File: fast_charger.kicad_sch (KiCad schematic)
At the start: 36 parts, among them J1 Screw_Terminal_01x02, J2 USB_A, J3 AVR-ISP-6, J4 Conn_02x08_Counter_Clockwise, Q1 PJD25N03, U1 CHY100, U2 IRS10752LVBF, U3 ATtiny404-SS, U4 AP7375, U5 AP7375, U6 INA180A4

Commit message: Completed BOM
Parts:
- removed C1, C2: C, symbol Device:C
- removed D1: D, symbol Device:D
- added C1: 10n, Capacitor_SMD:C_0603_1608Metric, symbol Device:C_Small
- added C10, C11, C9: 100u, Capacitor_SMD:CP_Elec_10x10.5, symbol Device:C_Polarized_US
- added D1: SBM54, Diode_SMD:D_SMA, symbol Device:D_Schottky
- added D3: RED, Diode_SMD:D_0603_1608Metric, symbol Device:LED
- added D4: YEL, Diode_SMD:D_0603_1608Metric, symbol Device:LED
- added D5: GRN, Diode_SMD:D_0603_1608Metric, symbol Device:LED
- added R13, R14, R15: 1k, Resistor_SMD:R_0603_1608Metric, symbol Device:R_US
- C3, C4, C5, C6, C7, C8: footprint (none) -> Capacitor_SMD:C_0603_1608Metric
- D2: value D_Schottky -> SBM54; footprint (none) -> Diode_SMD:D_SMA
- J1: footprint (none) -> TerminalBlock_Phoenix:TerminalBlock_Phoenix_MKDS-3-2-5.08_1x02_P5.08mm_Horizontal
- J2: footprint (none) -> fast_charger:usb_CU01
- J3: footprint (none) -> Connector_IDC:IDC-Header_2x03_P2.54mm_Vertical
- J4: footprint (none) -> Connector_PinHeader_1.27mm:PinHeader_1x16_P1.27mm_Vertical
- L1: value L -> 47u; footprint (none) -> fast_charger:L_murata_6000B
- R1, R10, R11, R2, R3, R5, R6, R7, R8, R9: footprint (none) -> Resistor_SMD:R_0603_1608Metric
- R12: value 25m -> 20m; footprint (none) -> Resistor_SMD:R_1206_3216Metric
- R4: value R_US -> 100k; footprint (none) -> Resistor_SMD:R_0603_1608Metric
- TP1, TP2: footprint (none) -> TestPoint:TestPoint_THTPad_D1.5mm_Drill0.7mm
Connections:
- net GND: now also C1.2, C10.2, C11.2, C9.2, D3.1 (K), D4.1 (K), D5.1 (K)
- net VDD: now also C9.1
- net at C4.1, C5.1, R6.1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: now also D1.2 (A)
- net VSW: now reaches C3.2, D2.1 (K), L1.1, Q1.2 (D), U2.4 (VS)
- net at L1.2, R12.1, U6.3 (+): now also C1.1, C10.1, C11.1
- net at C3.1, TP2.1, U2.6 (VB): now also D1.1 (K)
- net AUX_ANALOG: now reaches J4.16 (Pin_16)
- net ~{RST}: now reaches J3.5 (~{RST}), U3.10 (~{RESET}/PA0)
- net MOSI: now reaches J3.4 (MOSI), U3.11 (PA1)
- net MOSI: now also R14.1
- net MISO: now reaches J3.1 (MISO), U3.12 (PA2)
- net MISO: now also R13.1
- net SCK: now reaches J3.3 (SCK), U3.13 (PA3)
- net SCK: now also R15.1
- net SW renamed PWM
- new net: D4.2 (A), R14.2
- new net: D3.2 (A), R13.2
- new net: D5.2 (A), R15.2
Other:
- note added: "LEDs for diagnostics and communication"
- moved on the sheet: J1, J2, J3, R1, R12, R2, R3, R4, TP2, U1, U6

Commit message: Completed placement
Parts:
- added D6: SBM54, Diode_SMD:D_SMA, symbol Device:D_Schottky
- added J5: Conn_02x03_Odd_Even, Connector_PinHeader_1.27mm:PinHeader_2x03_P1.27mm_Vertical, symbol Connector_Generic:Conn_02x03_Odd_Even
- added Q2: PJD25N03, Package_TO_SOT_SMD:TO-252-2, symbol Device:Q_NMOS_GDS
- J4: value Conn_02x08_Counter_Clockwise -> Conn_02x08_Odd_Even; footprint Connector_PinHeader_1.27mm:PinHeader_1x16_P1.27mm_Vertical -> Connector_PinHeader_1.27mm:PinHeader_2x08_P1.27mm_Vertical; symbol Connector_Generic:Conn_02x08_Counter_Clockwise -> Connector_Generic:Conn_02x08_Odd_Even
- R1: value 100k -> 400k
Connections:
- net +5V: now also J5.1 (Pin_1), J5.3 (Pin_3), J5.5 (Pin_5); no longer R2.2, R3.2
- net AUX_ANALOG: now also J4.2 (Pin_2); no longer J4.16 (Pin_16)
- net GND: now also J5.2 (Pin_2), J5.4 (Pin_4), J5.6 (Pin_6), Q2.3 (S)
- net PWM: now also J4.16 (Pin_16); no longer J4.9 (Pin_9)
- net at C7.1, R8.2, R9.1: now also J4.8 (Pin_8); no longer J4.13 (Pin_13)
- net at C1.1, C10.1, C11.1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: now also D6.1 (K); no longer L1.2
- net at C8.1, R10.2, R11.1: now also J4.6 (Pin_6); no longer J4.14 (Pin_14)
- net at U3.3 (PA5): now also J4.3 (Pin_3); no longer J4.2 (Pin_2)
- net at U3.4 (PA6): now also J4.5 (Pin_5); no longer J4.3 (Pin_3)
- net at U3.5 (PA7): now also J4.7 (Pin_7); no longer J4.4 (Pin_4)
- net at U3.6 (PB3): now also J4.9 (Pin_9); no longer J4.5 (Pin_5)
- net at U3.7 (PB2): now also J4.11 (Pin_11); no longer J4.6 (Pin_6)
- net at U3.8 (PB1): now also J4.13 (Pin_13); no longer J4.7 (Pin_7)
- net at U3.9 (PB0): now also J4.15 (Pin_15); no longer J4.8 (Pin_8)
- net IL renamed ILOAD
- net ILOAD: now also J4.4 (Pin_4); no longer J4.15 (Pin_15)
- net ~{N1} renamed REQ_V
- net REQ_V: now also R3.2, U1.4 (V3); no longer U1.2 (V1)
- removed net ~{N2}: J4.11 (Pin_11), R2.1, U1.3 (V2)
- removed net ~{N3}: J4.12 (Pin_12), R3.1, U1.4 (V3)
- new net: D6.2 (A), L1.2, Q2.2 (D)
- new net: R2.1, U1.2 (V1)
- new net: R2.2, R3.1, U1.3 (V2)
- new net PWM2: J4.14 (Pin_14), Q2.1 (G)
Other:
- note added: "REQ_V | Requested Charge Voltage 5V | 5V 1.6V | 9V 1.0V | 12V 0V | 20V"
- moved on the sheet: C1, C10, C11, C3, C4, C5, C6, C7, C8, C9, D1, D2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

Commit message: V1 complete. PCB and parts ordered
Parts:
- D1: value SBM54 -> 1N4148W; footprint Diode_SMD:D_SMA -> Diode_SMD:D_SOD-123
- R6: value 100k -> 4.7k
- R7: value 200k -> 10k
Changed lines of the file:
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@@
       (effects (font (size 1.27 1.27)) (justify right))
     )
-    (property "Value" "SBM54" (at 152.4 86.6775 90)
-      (effects (font (size 1.27 1.27)) (justify right))
-    )
-    (property "Footprint" "Diode_SMD:D_SMA" (at 154.94 85.09 0)
+    (property "Value" "1N4148W" (at 152.4 86.6775 90)
+      (effects (font (size 1.27 1.27)) (justify right))
+    )
+    (property "Footprint" "Diode_SMD:D_SOD-123" (at 154.94 85.09 0)
       (effects (font (size 1.27 1.27)) hide)
     )
@@
       (effects (font (size 1.27 1.27)) (justify left))
     )
-    (property "Value" "200k" (at 125.73 96.52 0)
+    (property "Value" "10k" (at 125.73 96.52 0)
       (effects (font (size 1.27 1.27)) (justify left))
     )
@@
       (effects (font (size 1.27 1.27)) (justify left))
     )
-    (property "Value" "100k" (at 120.65 87.63 0)
-      (effects (font (size 1.27 1.27)) (justify left))
-    )
+    (property "Value" "4.7k" (at 120.65 87.63 0)
+      (effects (font (size 1.27 1.27)) (justify left))
+    )

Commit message: Too many issues. Moving to a simpler design
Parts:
- removed C5: 10n, Capacitor_SMD:C_0603_1608Metric, symbol Device:C_Small
- removed R6: 4.7k, Resistor_SMD:R_0603_1608Metric, symbol Device:R_US
- removed R7: 10k, Resistor_SMD:R_0603_1608Metric, symbol Device:R_US
- removed U4: AP7375, Package_TO_SOT_SMD:SOT-23, symbol Regulator_Linear:AP7384-28SA
- added D7, D8: 1N4148W, Diode_SMD:D_SOD-123, symbol Device:D_Schottky
- R10, R8: value 400k -> 100k
- R11, R9: value 100k -> 10k
- R12: value 20m -> 5m
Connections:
- net VBUS: now also D8.2 (A)
- net VDD: now also C4.1, D1.2 (A), TP1.1, U2.1 (VCC), D7.1 (K), D8.1 (K); no longer C9.1, J1.1 (Pin_1), Q1.3 (S)
- net VSW: now also Q1.3 (S); no longer Q1.2 (D)
- new net: C9.1, D7.2 (A), J1.1 (Pin_1), Q1.2 (D)
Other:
- note added: "Order of testing * Voltage regulators * High-side switch * Low-side switch * Voltage dividers * Current measurement * USB charge negotiation --- Firmware --- * High-side switch * Low-side switch * Analog inputs * Buck regulation * Boost regulation * Maximum power delivery"
- moved on the sheet: Q1

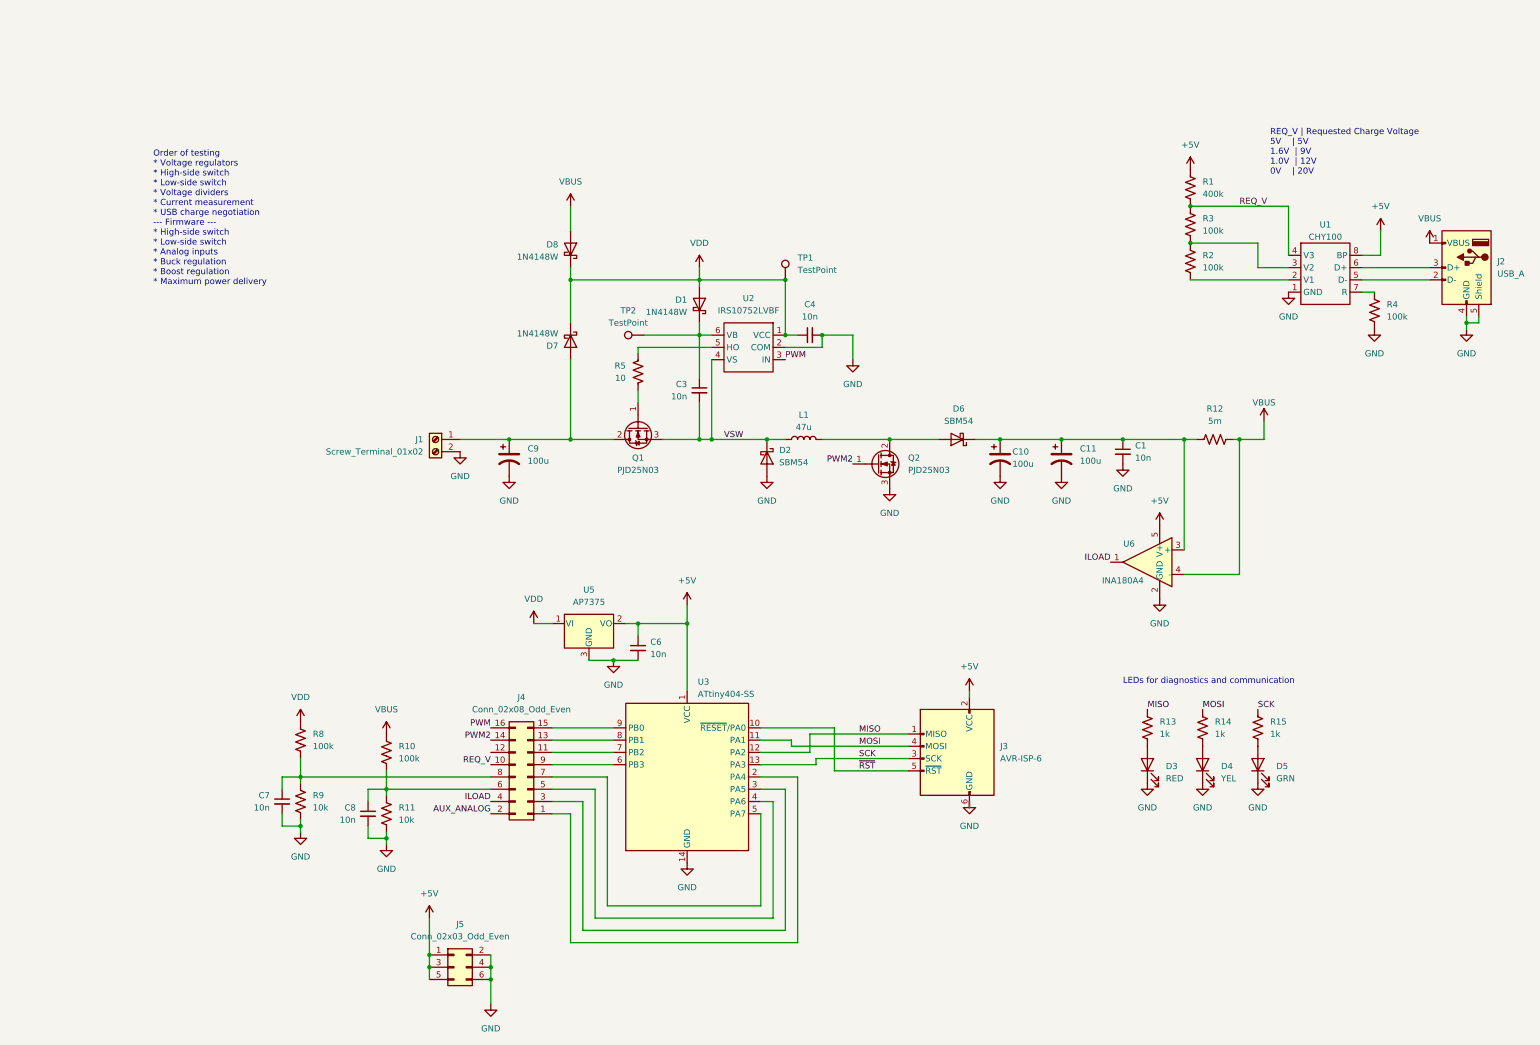
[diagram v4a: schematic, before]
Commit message: New simpler buck-only design
Bridge rectifier on input to allow reverse voltage
Voltage regulation is taken care of by ASIC
External microcontroller and OLED display show power/voltage/current
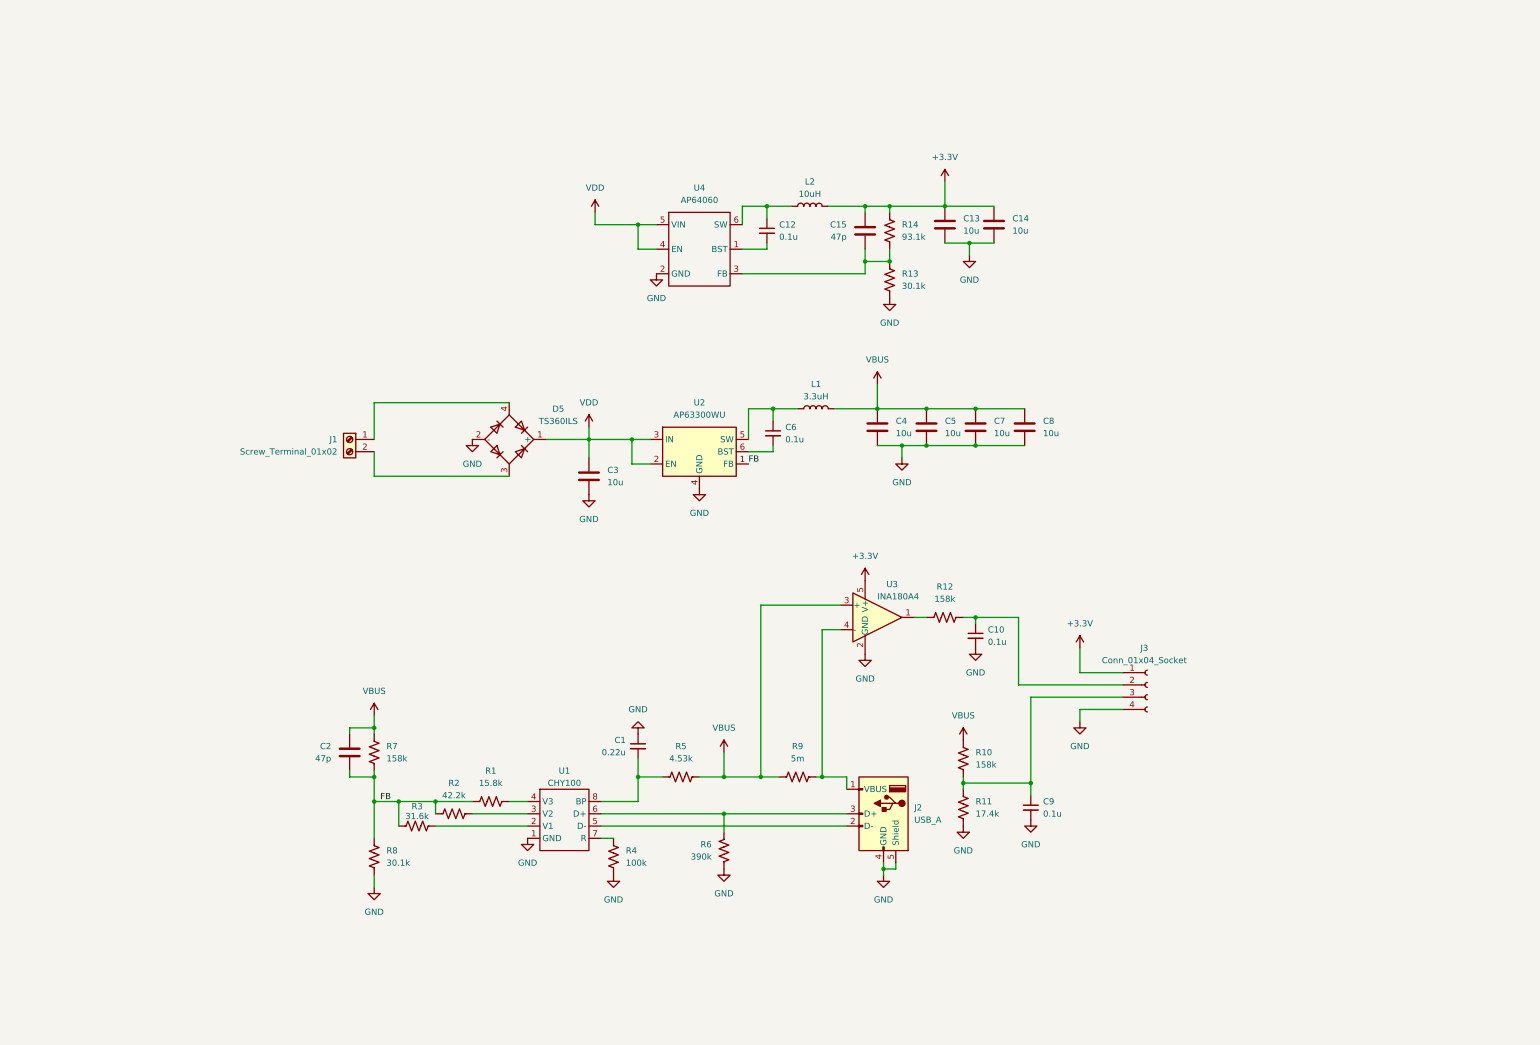
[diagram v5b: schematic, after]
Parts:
- removed C10, C11, C9: 100u, Capacitor_SMD:CP_Elec_10x10.5, symbol Device:C_Polarized_US
- removed C3, C4, C7, C8: 10n, Capacitor_SMD:C_0603_1608Metric, symbol Device:C_Small
- removed D1, D7, D8: 1N4148W, Diode_SMD:D_SOD-123, symbol Device:D_Schottky
- removed D2, D6: SBM54, Diode_SMD:D_SMA, symbol Device:D_Schottky
- removed D3: RED, Diode_SMD:D_0603_1608Metric, symbol Device:LED
- removed D4: YEL, Diode_SMD:D_0603_1608Metric, symbol Device:LED
- removed D5: GRN, Diode_SMD:D_0603_1608Metric, symbol Device:LED
- removed J3: AVR-ISP-6, Connector_IDC:IDC-Header_2x03_P2.54mm_Vertical, symbol Connector:AVR-ISP-6
- removed J4: Conn_02x08_Odd_Even, Connector_PinHeader_1.27mm:PinHeader_2x08_P1.27mm_Vertical, symbol Connector_Generic:Conn_02x08_Odd_Even
- removed J5: Conn_02x03_Odd_Even, Connector_PinHeader_1.27mm:PinHeader_2x03_P1.27mm_Vertical, symbol Connector_Generic:Conn_02x03_Odd_Even
- removed Q1, Q2: PJD25N03, Package_TO_SOT_SMD:TO-252-2, symbol Device:Q_NMOS_GDS
- removed R15: 1k, Resistor_SMD:R_0603_1608Metric, symbol Device:R_US
- removed TP1, TP2: TestPoint, TestPoint:TestPoint_THTPad_D1.5mm_Drill0.7mm, symbol Connector:TestPoint
- removed U2: IRS10752LVBF, Package_TO_SOT_SMD:SOT-23-6, symbol fast_charger:gate_driver
- removed U3: ATtiny404-SS, Package_SO:SOIC-14_3.9x8.7mm_P1.27mm, symbol MCU_Microchip_ATtiny:ATtiny404-SS
- removed U5: AP7375, Package_TO_SOT_SMD:SOT-23, symbol Regulator_Linear:AP7384-28SA
- removed U6: INA180A4, Package_TO_SOT_SMD:SOT-23-5, symbol Amplifier_Current:INA180A4
- added C10, C12, C9: 0.1u, Capacitor_SMD:C_0603_1608Metric, symbol Device:C_Small
- added C13, C14: 10u, Capacitor_SMD:C_0805_2012Metric, symbol Device:C
- added C15, C2: 47p, Capacitor_SMD:C_0603_1608Metric, symbol Device:C
- added C3, C4, C5, C7, C8: 10u, Capacitor_SMD:C_1206_3216Metric, symbol Device:C
- added D5: TS360ILS, Package_SO:TSSOP-4_4.4x5mm_P4mm, symbol Diode_Bridge:MDB6S
- added J3: Conn_01x04_Socket, Connector_PinHeader_2.54mm:PinHeader_1x04_P2.54mm_Vertical, symbol Connector:Conn_01x04_Socket
- added L2: 10uH, Inductor_SMD:L_0805_2012Metric, symbol Device:L
- added R6: 390k, Resistor_SMD:R_0603_1608Metric, symbol Device:R_US
- added R7: 158k, Resistor_SMD:R_0603_1608Metric, symbol Device:R_US
- added U2: AP63300WU, Package_TO_SOT_SMD:TSOT-23-6, symbol Regulator_Switching:AP63200WU
- added U3: INA180A4, Package_TO_SOT_SMD:SOT-23-5, symbol Amplifier_Current:INA180A4
- added U4: AP64060, Package_TO_SOT_SMD:SOT-23-6, symbol fast_charger:AP64060
- C1: value 10n -> 0.22u
- C6: value 10n -> 0.1u
- L1: value 47u -> 3.3uH; footprint fast_charger:L_murata_6000B -> fast_charger:L_6.5x6.5
- R1: value 400k -> 15.8k
- R10: value 100k -> 158k
- R11: value 10k -> 17.4k
- R12: value 5m -> 158k; footprint Resistor_SMD:R_1206_3216Metric -> Resistor_SMD:R_0603_1608Metric
- R13: value 1k -> 30.1k
- R14: value 1k -> 93.1k
- R2: value 100k -> 42.2k
- R3: value 100k -> 31.6k
- R5: value 10 -> 4.53k
- R8: value 100k -> 30.1k
- R9: value 10k -> 5m; footprint Resistor_SMD:R_0603_1608Metric -> Resistor_SMD:R_0805_2012Metric
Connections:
- net MISO is gone; now on an unnamed net: R13.1
- net GND: now also C1.1, R11.1, R13.2, R8.2, C10.2, C13.2, C14.2, C3.2, C4.2, C5.2, C7.2, C8.2, C9.2, D5.2 (-), J3.4 (Pin_4), R6.1, U2.4 (GND), U3.2 (GND), U4.2 (GND); no longer C1.2, C6.2, J1.2 (Pin_2), R11.2, R9.2
- net VBUS: now also L1.2, R5.2, R9.1, C2.1, C4.1, C5.1, C7.1, C8.1, R7.1, U3.3 (+); no longer J2.1 (VBUS), R12.2
- net VDD: now also C3.1, D5.1 (+), U2.2 (EN), U2.3 (IN), U4.4 (EN), U4.5 (VIN); no longer R8.1
- net at J1.1 (Pin_1): now also D5.4
- net at J2.3 (D+), U1.6 (D+): now also R6.2
- net at R14.2: now also C15.2, U4.3 (FB)
- net at R5.1: now also C1.2, U1.8 (BP)
- net at R10.2: now also R11.2, C9.1, J3.3 (Pin_3); no longer R11.1
- net at R12.1: now also U3.1; no longer C1.1
- net at U1.2 (V1): now also R3.2; no longer R2.1
- net at R2.2, U1.3 (V2): no longer R3.1
- removed net +5V: C6.1, R1.2, U1.8 (BP)
- net MOSI renamed +3.3V
- net +3.3V: now also C13.1, C14.1, C15.1, J3.1 (Pin_1), L2.2, U3.5 (V+)
- removed net REQ_V: R1.1, R3.2, U1.4 (V3)
- net VSW: no longer names the net of L1.1
- net VSW: now also C6.1, U2.5 (SW)
- new net: J2.1 (VBUS), R9.2, U3.4 (-)
- new net: C10.1, J3.2 (Pin_2), R12.2
- new net: C12.2, U4.1 (BST)
- new net: C12.1, L2.1, U4.6 (SW)
- new net: C6.2, U2.6 (BST)
- new net: R1.2, U1.4 (V3)
- new net: D5.3, J1.2 (Pin_2)
- new net FB: C2.2, R1.1, R2.1, R3.1, R7.2, R8.1, U2.1 (FB)
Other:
- note removed: "LEDs for diagnostics and communication"
- note removed: "Order of testing * Voltage regulators * High-side switch * Low-side switch * Voltage dividers * Current measurement * USB charge negotiation --- Firmware --- * High-side switch * Low-side switch * Analog inputs * Buck regulation * Boost regulation * Maximum power delivery"
- note removed: "REQ_V | Requested Charge Voltage 5V | 5V 1.6V | 9V 1.0V | 12V 0V | 20V"
- moved on the sheet: J1, J2, R4, U1
